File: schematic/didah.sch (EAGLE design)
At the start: 20 parts, among them T1 TEENSY_3.0_ALLPINS

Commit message: Added URL. Created PDF from schematic.
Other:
- note added: "http://pictographer.com/didah"
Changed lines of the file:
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@@
 <text x="17.78" y="2.54" size="1.778" layer="91">dahPin</text>
 <text x="20.32" y="63.5" size="1.778" layer="91">earphoneRightPin</text>
+<text x="101.6" y="-7.62" size="1.778" layer="91">http://pictographer.com/didah</text>
 </plain>
 <instances>

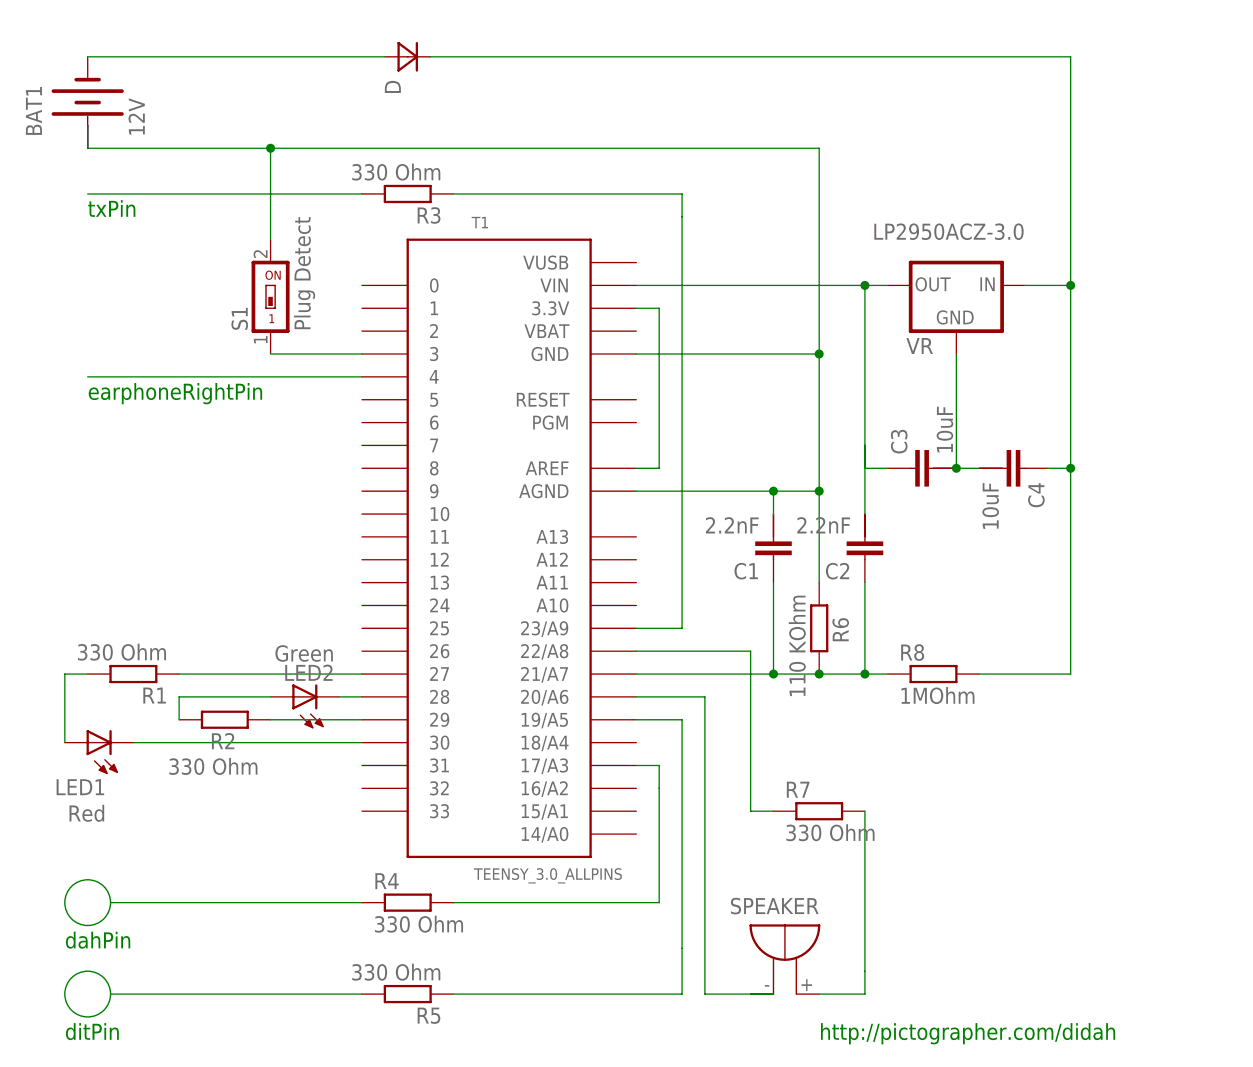
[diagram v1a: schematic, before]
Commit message: Added Transmit Enable (TE)
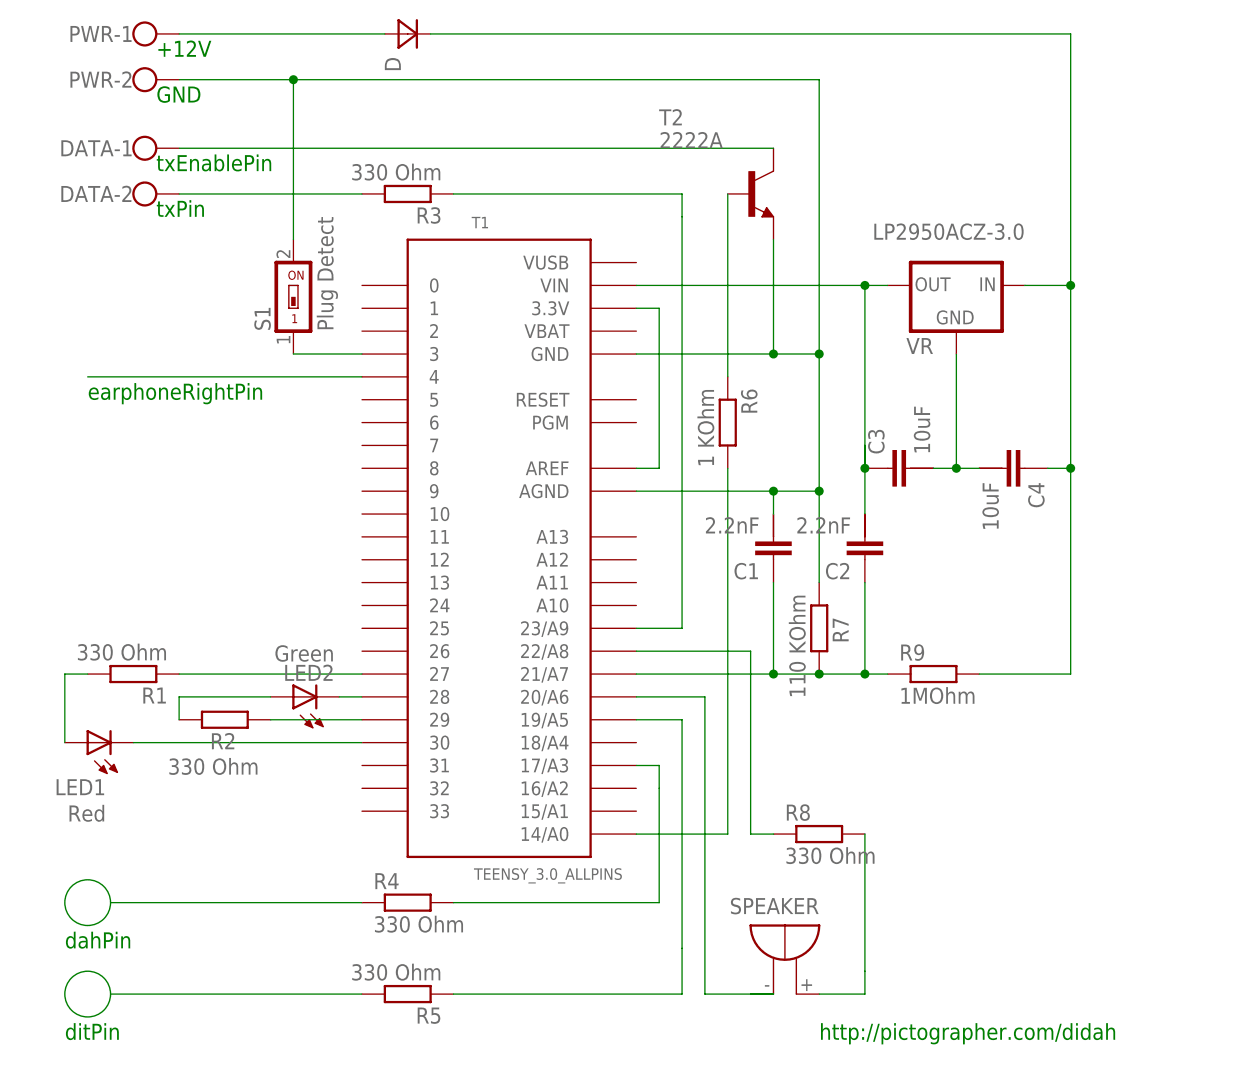
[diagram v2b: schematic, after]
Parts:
- removed BAT1: 12V, special:BATTERY
- added DATA, PWR: (no value), con-wago-500:W237-102
- added R9: 1MOhm, eagle-ltspice:R0204/7
- added T2: 2222A, transistor-neu-to92:2N2222-NPN-TO92-EBC
- R6: value 110 KOhm -> 1 KOhm; device eagle-ltspice:R0204/7 -> eagle-ltspice:RR0402
- R7: value 330 Ohm -> 110 KOhm; device eagle-ltspice:RR0402 -> eagle-ltspice:R0204/7
- R8: value 1MOhm -> 330 Ohm; device eagle-ltspice:R0204/7 -> eagle-ltspice:RR0402
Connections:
- removed net N$4: BAT1.-, D.C
- new net N$25: R6.2, T1.14/A0
- new net N$26: DATA-1.KL, T2.C
- new net N$27: R6.1, T2.B
- new net N$28: C1.2, PWR-2.KL, R7.1, S1.2, T1.AGND, T1.GND, T2.E
- net N$11: now also R7.2, R9.1; no longer R6.2, R8.1
- net N$12: now also D.C, PWR-1.KL; no longer BAT1.+, BAT1.+@1, C1.2, R6.1, S1.2, T1.AGND, T1.GND
- net N$13: now also R8.2; no longer R7.2
- net N$16: now also R8.1; no longer R7.1
- net N$20: now also DATA-2.KL
- net N$9: now also R9.2; no longer R8.2
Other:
- note added: "+12V"
- note added: "GND"
- note added: "txEnablePin"
- moved on the sheet: C3, D, R6, R7, R8, S1
